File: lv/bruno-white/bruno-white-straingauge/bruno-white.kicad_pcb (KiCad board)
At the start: 2 copper layers, 5 parts, among them U1 INA128

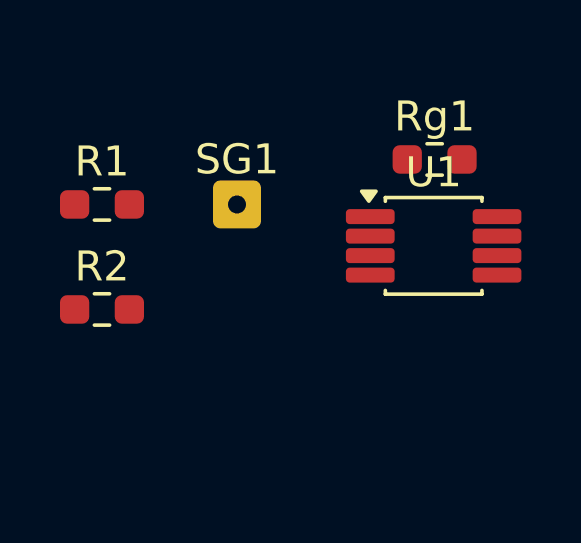
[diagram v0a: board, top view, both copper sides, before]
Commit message: Low Voltage DONE
I have added a reference voltage device and an op amp buffer to my IN amp in order to match the output voltage from the wheatstone bridge circuit. I researched these two devices and I will continue to in order to better understand how they work... Lastly, I have added the link to my google doc which will have all my physical notes. Thank you for your consideration and I hope to join!
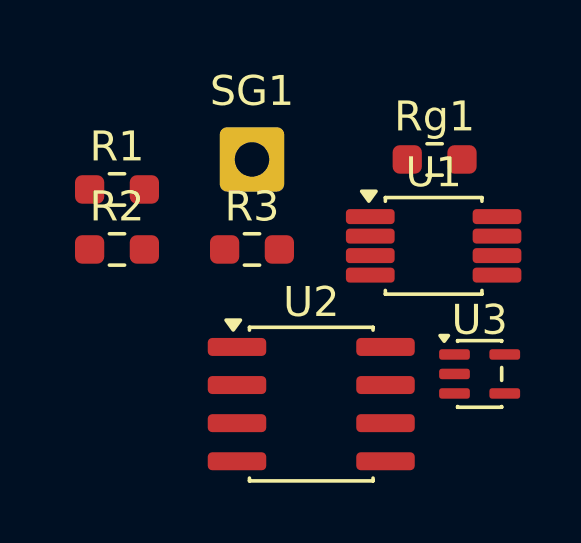
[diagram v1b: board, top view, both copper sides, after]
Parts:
- added R3: 350ohm, Resistor_SMD:R_0603_1608Metric_Pad0.98x0.95mm_HandSolder, F.Cu at (148.5, 94.5)
- added U2: VRef, Package_SO:SOIC-8_3.9x4.9mm_P1.27mm, F.Cu at (150.5, 99.7)
- added U3: Op amp buffer, Package_TO_SOT_SMD:SOT-353_SC-70-5, F.Cu at (156.1, 98.7)
- R1, R2: value R_Small -> 350ohm
- Rg1: value ??? -> 100ohm(500gain)
- SG1: footprint Connector_Wire:SolderWire-0.1sqmm_1x01_D0.4mm_OD1mm -> Connector_Wire:SolderWire-0.5sqmm_1x01_D0.9mm_OD2.1mm
- moved R2 2.06 mm to (144.0, 94.5)
- moved SG1 1.58 mm to (148.5, 91.5)
- moved R1 0.71 mm to (144.0, 92.5)
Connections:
- R1 pad 2: +5V -> Vb
- U1 pad 4: unconnected-(U1-V--Pad4) -> -5V
- U1 pad 5: GNDREF -> /2.5V
- U1 pad 7: unconnected-(U1-V+-Pad7) -> Vb
